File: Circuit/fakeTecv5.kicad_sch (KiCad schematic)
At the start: 31 parts, among them J11 T1 3,3, J12 T2 3,3, J13 T3 3,3, J14 GPS Pins, J16 Encoder Pins, J5 I2C Oled screen, J6 FET1 Drain, J7 FET2 Drain, J8 FET3 Drain, J9 Battery Connector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

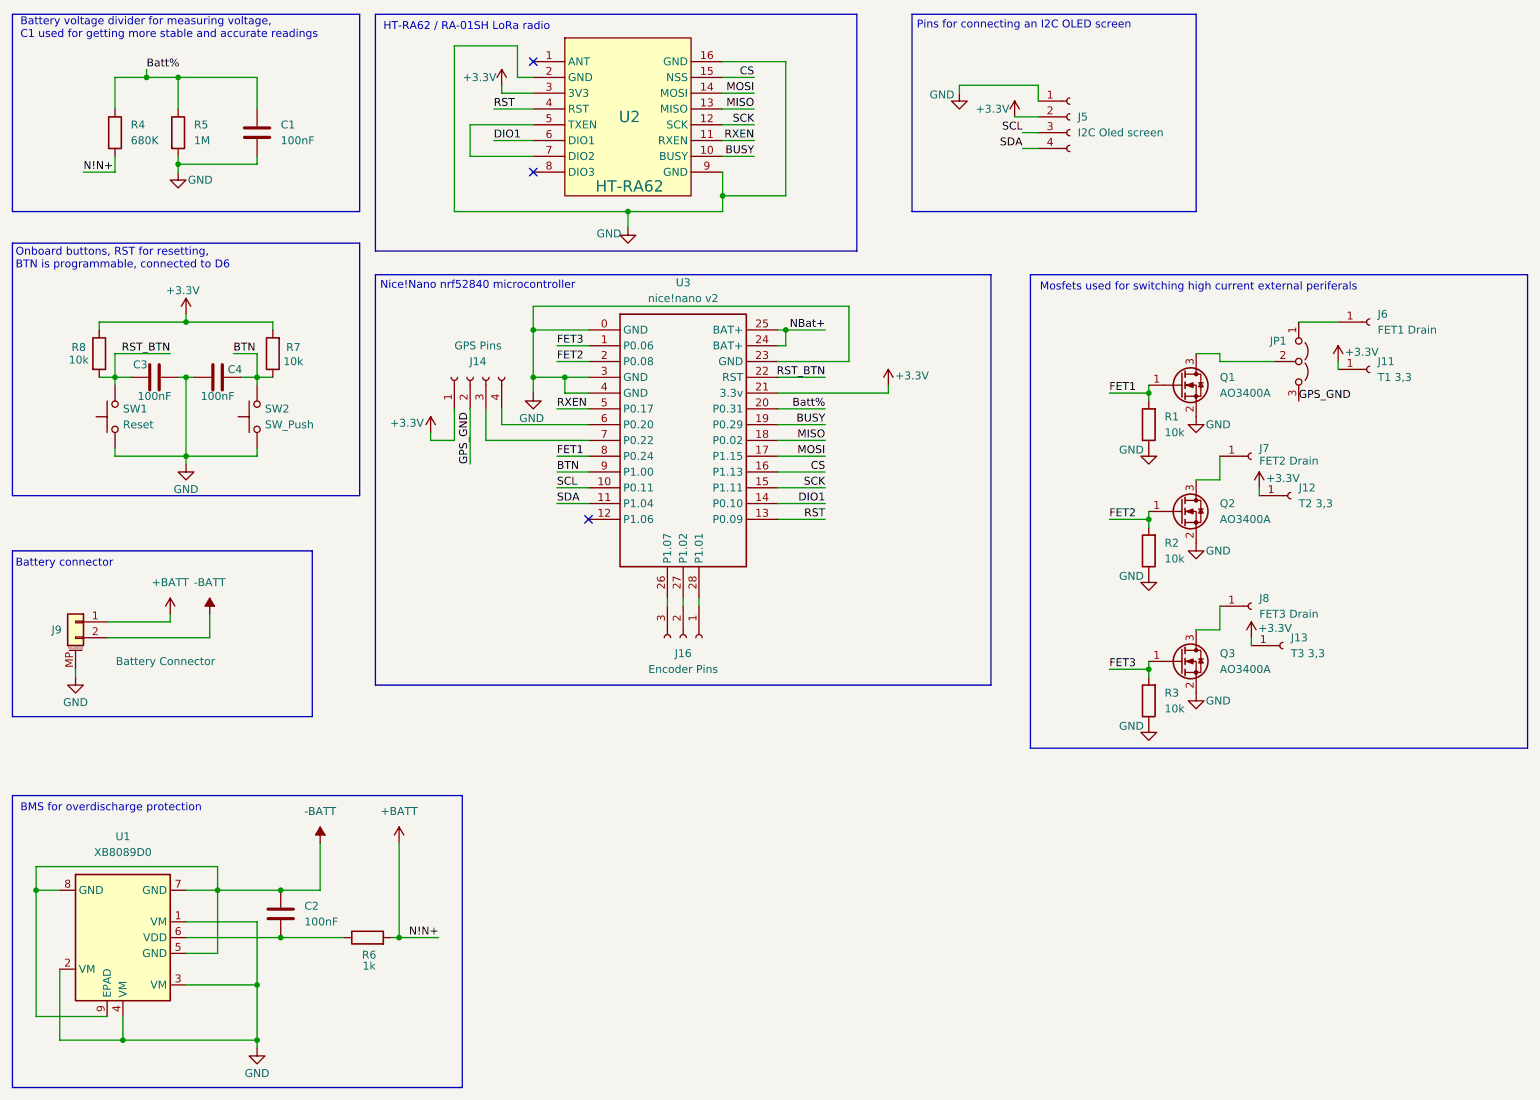
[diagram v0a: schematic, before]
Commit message: Added pull up resistors and ground pad to rotary encoder pads
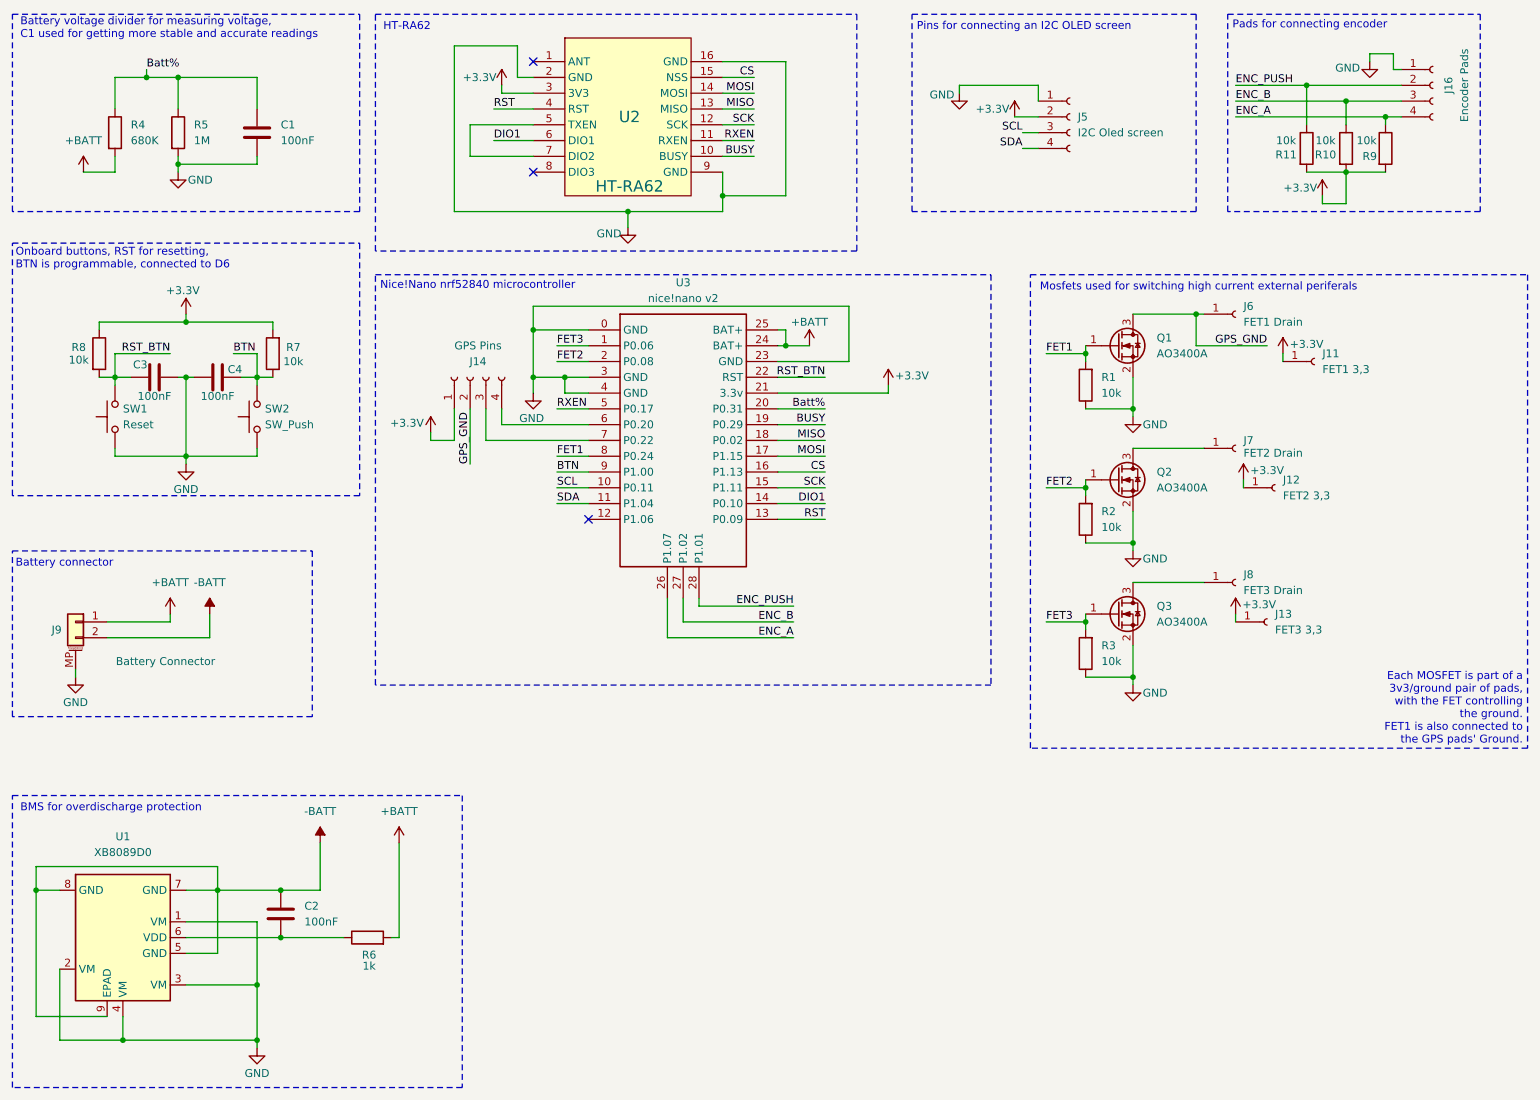
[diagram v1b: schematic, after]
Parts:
- removed JP1: (no value), Jumper:SolderJumper-3_P1.3mm_Open_RoundedPad1.0x1.5mm, symbol Jumper:Jumper_3_Open
- added R10, R11, R9: 10k, Resistor_SMD:R_0805_2012Metric_Pad1.20x1.40mm_HandSolder, symbol Device:R
- J11: value T1 3,3 -> FET1 3,3; footprint SMD_PAD:SMD_PAD_1x1 -> SMD_PAD:SMD_PAD_1x01
- J12: value T2 3,3 -> FET2 3,3; footprint SMD_PAD:SMD_PAD_1x1 -> SMD_PAD:SMD_PAD_1x01
- J13: value T3 3,3 -> FET3 3,3; footprint SMD_PAD:SMD_PAD_1x1 -> SMD_PAD:SMD_PAD_1x01
- J14: footprint SMD_PAD:SMD_PAD_4x1 -> SMD_PAD:SMD_PAD_1x04
- J16: value Encoder Pins -> Encoder Pads; footprint SMD_PAD:SMD_PAD_3x1 -> SMD_PAD:SMD_PAD_1x04; symbol Connector:Conn_01x03_Socket -> Connector:Conn_01x04_Socket
- J6, J7, J8: footprint SMD_PAD:SMD_PAD_1x1 -> SMD_PAD:SMD_PAD_1x01
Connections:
- net NBat+ is gone; now on net +BATT: U3.24 (BAT+), U3.25 (BAT+)
- net +3.3V: now also R10.2, R11.2, R9.2
- net GND: now also J16.1 (Pin_1)
- net GPS_GND: now also J6.1 (Pin_1), Q1.3 (D)
- net ENC_A: now reaches U3.26 (P1.07)
- net ENC_A: now also J16.4 (Pin_4), R9.1; no longer J16.3 (Pin_3)
- net ENC_B: now reaches U3.27 (P1.02)
- net ENC_B: now also J16.3 (Pin_3), R10.1; no longer J16.2 (Pin_2)
- net ENC_PUSH: now reaches U3.28 (P1.01)
- net ENC_PUSH: now also J16.2 (Pin_2), R11.1; no longer J16.1 (Pin_1)
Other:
- note added: "Each MOSFET is part of a 3v3/ground pair of pads, with the FET controlling the ground. FET1 is also connected to the GPS pads' Ground."
- note added: "HT-RA62"
- note added: "Pads for connecting encoder"
- note removed: "HT-RA62 / RA-01SH LoRa radio"
- moved on the sheet: J11, J12, J13, J6, J7, J8, Q1, Q2, Q3, R1, R2, R3
